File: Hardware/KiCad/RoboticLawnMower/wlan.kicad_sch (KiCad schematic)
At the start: 1 part, among them U3 ESP32-WROOM-32D

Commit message: Layout
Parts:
- added J16, J17: Conn_01x04, Connector_JST:JST_XA_B04B-XASK-1-A_1x04_P2.50mm_Vertical, symbol Connector_Generic:Conn_01x04
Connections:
- net GND: now reaches U3.1 (GND), U3.15 (GND), U3.38 (GND), U3.39 (GND)
- net GND: now also J16.4 (Pin_4), J17.4 (Pin_4)
- net RGB_LED_1: now reaches U3.13 (IO14)
- net RGB_LED_1: now also J17.3 (Pin_3)
- net RGB_LED_0: now reaches U3.16 (IO13)
- net RGB_LED_0: now also J17.2 (Pin_2)
- net +3.3V: now reaches U3.2 (VDD)
- net +3.3V: now also J16.1 (Pin_1), J17.1 (Pin_1)
- net at U3.26 (IO4): now also J16.2 (Pin_2)
- net at U3.29 (IO5): now also J16.3 (Pin_3)
- net UART_TxD_uC: now reaches U3.34 (RXD0/IO3)
- net UART_RxD_uC: now reaches U3.35 (TXD0/IO1)
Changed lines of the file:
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@@
 (kicad_sch (version 20211123) (generator eeschema)
   (paper "A3")
+  (junction (at 208.28 81.28) (diameter 0) (color 0 0 0 0)
+  )
+  (junction (at 209.55 59.69) (diameter 0) (color 0 0 0 0)
+  )
+  (wire (pts (xy 167.64 76.2) (xy 212.09 76.2))
+    (stroke (width 0) (type default) (color 0 0 0 0))
+  )
+  (wire (pts (xy 209.55 59.69) (xy 209.55 73.66))
+    (stroke (width 0) (type default) (color 0 0 0 0))
+  )
+  (wire (pts (xy 123.19 41.91) (xy 123.19 46.99))
+    (stroke (width 0) (type default) (color 0 0 0 0))
+  )
+  (wire (pts (xy 212.09 73.66) (xy 209.55 73.66))
+    (stroke (width 0) (type default) (color 0 0 0 0))
+  )
+  (wire (pts (xy 138.43 64.77) (xy 212.09 64.77))
+    (stroke (width 0) (type default) (color 0 0 0 0))
+  )
+  (wire (pts (xy 138.43 62.23) (xy 212.09 62.23))
+    (stroke (width 0) (type default) (color 0 0 0 0))
+  )
+  (wire (pts (xy 138.43 54.61) (xy 162.56 54.61))
+    (stroke (width 0) (type default) (color 0 0 0 0))
+  )
+  (wire (pts (xy 138.43 69.85) (xy 167.64 69.85))
+    (stroke (width 0) (type default) (color 0 0 0 0))
+  )
+  (wire (pts (xy 209.55 59.69) (xy 212.09 59.69))
+    (stroke (width 0) (type default) (color 0 0 0 0))
+  )
+  (wire (pts (xy 165.1 78.74) (xy 212.09 78.74))
+    (stroke (width 0) (type default) (color 0 0 0 0))
+  )
+  (wire (pts (xy 212.09 67.31) (xy 208.28 67.31))
+    (stroke (width 0) (type default) (color 0 0 0 0))
+  )
+  (wire (pts (xy 167.64 69.85) (xy 167.64 76.2))
+    (stroke (width 0) (type default) (color 0 0 0 0))
+  )
+  (wire (pts (xy 138.43 72.39) (xy 165.1 72.39))
+    (stroke (width 0) (type default) (color 0 0 0 0))
+  )
+  (wire (pts (xy 208.28 81.28) (xy 208.28 83.82))
+    (stroke (width 0) (type default) (color 0 0 0 0))
+  )
+  (wire (pts (xy 165.1 72.39) (xy 165.1 78.74))
+    (stroke (width 0) (type default) (color 0 0 0 0))
+  )
+  (wire (pts (xy 208.28 67.31) (xy 208.28 81.28))
+    (stroke (width 0) (type default) (color 0 0 0 0))
+  )
+  (wire (pts (xy 209.55 55.88) (xy 209.55 59.69))
+    (stroke (width 0) (type default) (color 0 0 0 0))
+  )
+  (wire (pts (xy 138.43 59.69) (xy 162.56 59.69))
+    (stroke (width 0) (type default) (color 0 0 0 0))
+  )
+  (wire (pts (xy 208.28 81.28) (xy 212.09 81.28))
+    (stroke (width 0) (type default) (color 0 0 0 0))
+  )
+  (label "RGB_LED_0" (at 172.72 76.2 0)
+    (effects (font (size 1.27 1.27)) (justify left bottom))
+  )
+  (label "RGB_LED_1" (at 172.72 78.74 0)
+    (effects (font (size 1.27 1.27)) (justify left bottom))
+  )
+  (hierarchical_label "UART_TxD_uC" (shape input) (at 162.56 59.69 0)
+    (effects (font (size 1.27 1.27)) (justify left))
+  )
+  (hierarchical_label "UART_RxD_uC" (shape input) (at 162.56 54.61 0)
+    (effects (font (size 1.27 1.27)) (justify left))
+  )
+  (symbol (lib_id "power:GND") (at 123.19 118.11 0) (unit 1)
+    (in_bom yes) (on_board yes) (fields_autoplaced)
+    (property "Reference" "#PWR087" (id 0) (at 123.19 124.46 0)
+      (effects (font (size 1.27 1.27)) hide)
+    )
+    (property "Value" "GND" (id 1) (at 123.19 123.19 0))
+    (property "Footprint" "" (id 2) (at 123.19 118.11 0)
+      (effects (font (size 1.27 1.27)) hide)
+    )
+    (property "Datasheet" "" (id 3) (at 123.19 118.11 0)
+      (effects (font (size 1.27 1.27)) hide)
+    )
+    (pin "1")
+  )
+  (symbol (lib_id "power:+3.3V") (at 209.55 55.88 0) (unit 1)
+    (in_bom yes) (on_board yes) (fields_autoplaced)
+    (property "Reference" "#PWR089" (id 0) (at 209.55 59.69 0)
+      (effects (font (size 1.27 1.27)) hide)
+    )
+    (property "Value" "+3.3V" (id 1) (at 209.55 50.8 0))
+    (property "Footprint" "" (id 2) (at 209.55 55.88 0)
+      (effects (font (size 1.27 1.27)) hide)
+    )
+    (property "Datasheet" "" (id 3) (at 209.55 55.88 0)
+      (effects (font (size 1.27 1.27)) hide)
+    )
+    (pin "1")
+  )
+  (symbol (lib_id "power:GND") (at 208.28 83.82 0) (unit 1)
+    (in_bom yes) (on_board yes) (fields_autoplaced)
+    (property "Reference" "#PWR088" (id 0) (at 208.28 90.17 0)
+      (effects (font (size 1.27 1.27)) hide)
+    )
+    (property "Value" "GND" (id 1) (at 208.28 88.9 0))
+    (property "Footprint" "" (id 2) (at 208.28 83.82 0)
+      (effects (font (size 1.27 1.27)) hide)
+    )
+    (property "Datasheet" "" (id 3) (at 208.28 83.82 0)
+      (effects (font (size 1.27 1.27)) hide)
+    )
+    (pin "1")
+  )
+  (symbol (lib_id "Connector_Generic:Conn_01x04") (at 217.17 76.2 0) (unit 1)
+    (in_bom yes) (on_board yes) (fields_autoplaced)
+    (property "Reference" "J17" (id 0) (at 219.71 76.1999 0)
+      (effects (font (size 1.27 1.27)) (justify left))
+    )
+    (property "Value" "Conn_01x04" (id 1) (at 219.71 78.7399 0)
+      (effects (font (size 1.27 1.27)) (justify left))
+    )
+    (property "Footprint" "Connector_JST:JST_XA_B04B-XASK-1-A_1x04_P2.50mm_Vertical" (id 2) (at 217.17 76.2 0)
+      (effects (font (size 1.27 1.27)) hide)
+    )
+    (property "Datasheet" "~" (id 3) (at 217.17 76.2 0)
+      (effects (font (size 1.27 1.27)) hide)
+    )
+    (pin "1")
+    (pin "2")
+    (pin "3")
+    (pin "4")
+  )
+  (symbol (lib_id "Connector_Generic:Conn_01x04") (at 217.17 62.23 0) (unit 1)
+    (in_bom yes) (on_board yes) (fields_autoplaced)
+    (property "Reference" "J16" (id 0) (at 219.71 62.2299 0)
+      (effects (font (size 1.27 1.27)) (justify left))
+    )
+    (property "Value" "Conn_01x04" (id 1) (at 219.71 64.7699 0)
+      (effects (font (size 1.27 1.27)) (justify left))
+    )
+    (property "Footprint" "Connector_JST:JST_XA_B04B-XASK-1-A_1x04_P2.50mm_Vertical" (id 2) (at 217.17 62.23 0)
+      (effects (font (size 1.27 1.27)) hide)
+    )
+    (property "Datasheet" "~" (id 3) (at 217.17 62.23 0)
+      (effects (font (size 1.27 1.27)) hide)
+    )
+    (pin "1")
+    (pin "2")
+    (pin "3")
+    (pin "4")
+  )
+  (symbol (lib_id "power:+3.3V") (at 123.19 41.91 0) (unit 1)
+    (in_bom yes) (on_board yes) (fields_autoplaced)
+    (property "Reference" "#PWR086" (id 0) (at 123.19 45.72 0)
+      (effects (font (size 1.27 1.27)) hide)
+    )
+    (property "Value" "+3.3V" (id 1) (at 123.19 36.83 0))
+    (property "Footprint" "" (id 2) (at 123.19 41.91 0)
+      (effects (font (size 1.27 1.27)) hide)
+    )
+    (property "Datasheet" "" (id 3) (at 123.19 41.91 0)
+      (effects (font (size 1.27 1.27)) hide)
+    )
+    (pin "1")
+  )
   (symbol (lib_id "RF_Module:ESP32-WROOM-32D") (at 123.19 82.55 0) (unit 1)
     (in_bom yes) (on_board yes) (fields_autoplaced)

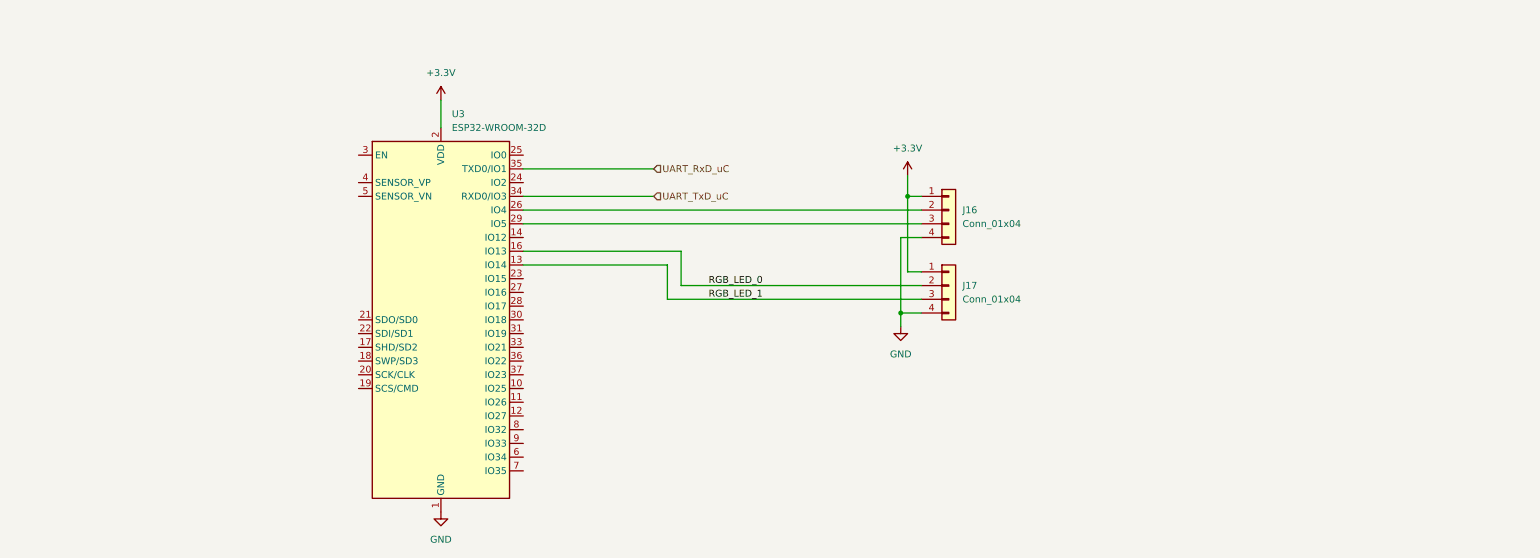
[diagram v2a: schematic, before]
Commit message: Schaltplan und Layout änderung
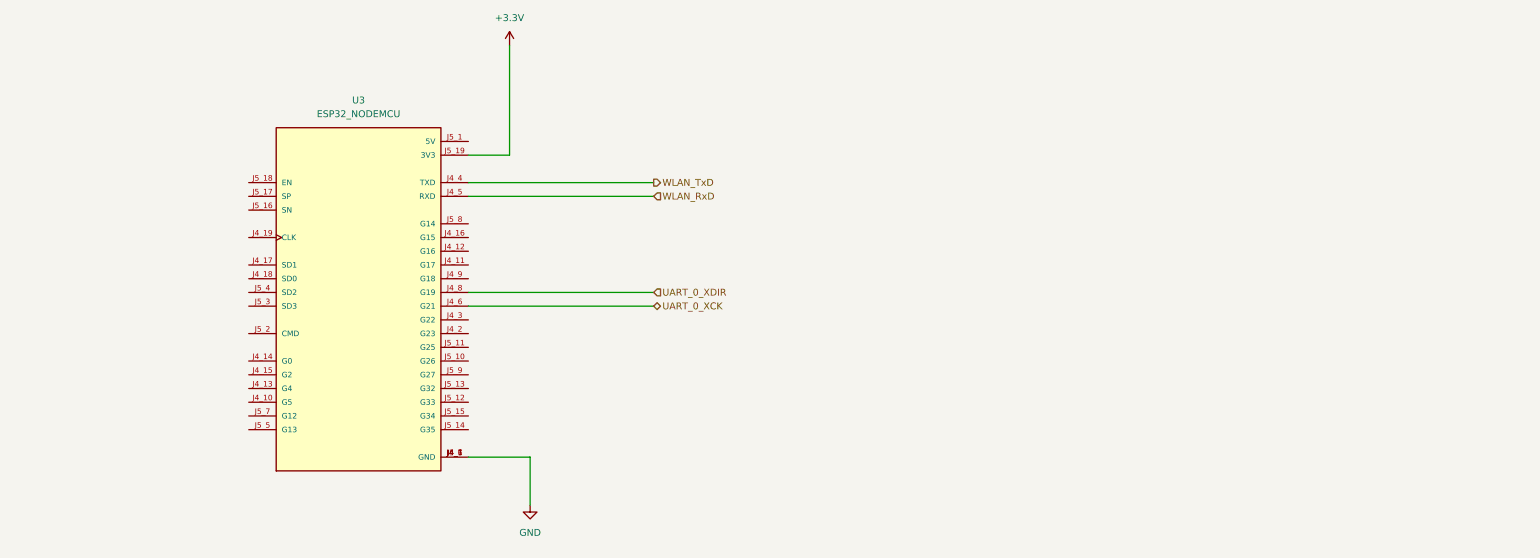
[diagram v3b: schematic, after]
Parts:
- removed J16, J17: Conn_01x04, Connector_JST:JST_XA_B04B-XASK-1-A_1x04_P2.50mm_Vertical, symbol Connector_Generic:Conn_01x04
- removed U3: ESP32-WROOM-32D, RF_Module:ESP32-WROOM-32, symbol RF_Module:ESP32-WROOM-32D
- added U3: ESP32_NODEMCU, MODULE_ESP32_NODEMCU, symbol ESP32_NODEMCU:ESP32_NODEMCU
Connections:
- net +3.3V: now also U3.J5_19 (3V3)
- net GND: now also U3.J4_1 (GND), U3.J4_7 (GND), U3.J5_6 (GND)
- new net UART_0_XCK: U3.J4_6 (G21)
- new net UART_0_XDIR: U3.J4_8 (G19)
- new net WLAN_RxD: U3.J4_5 (RXD)
- new net WLAN_TxD: U3.J4_4 (TXD)

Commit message: Layout
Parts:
- removed U3: ESP32_NODEMCU, MODULE_ESP32_NODEMCU, symbol ESP32_NODEMCU:ESP32_NODEMCU
- added U3: mini_esp32, ESP32_mini:ESP32_mini, symbol ESP_WEMOS_D1:mini_esp32
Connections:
- net +3.3V: now also U3.16 (3V3)
- net GND: now also U3.1 (GND), U3.22 (GND), U3.33 (GND)
- net UART_0_XCK: now also U3.28 (IO_32)
- net UART_0_XDIR: now also U3.24 (IO_27)
- net WLAN_RxD: now also U3.23 (RXD)
- net WLAN_TxD: now also U3.21 (TXD)
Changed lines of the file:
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@@
 (kicad_sch (version 20211123) (generator eeschema)
   (paper "A3")
-  (wire (pts (xy 128.27 77.47) (xy 162.56 77.47))
+  (junction (at 125.73 57.15) (diameter 0) (color 0 0 0 0)
+  )
+  (junction (at 125.73 59.69) (diameter 0) (color 0 0 0 0)
+  )
+  (wire (pts (xy 93.98 110.49) (xy 59.69 110.49))
     (stroke (width 0) (type default) (color 0 0 0 0))
   )
-  (wire (pts (xy 139.7 116.84) (xy 139.7 107.95))
+  (wire (pts (xy 125.73 59.69) (xy 125.73 116.84))
     (stroke (width 0) (type default) (color 0 0 0 0))
   )
-  (wire (pts (xy 135.89 31.75) (xy 135.89 52.07))
+  (wire (pts (xy 120.65 57.15) (xy 125.73 57.15))
     (stroke (width 0) (type default) (color 0 0 0 0))
   )
-  (wire (pts (xy 128.27 80.01) (xy 162.56 80.01))
+  (wire (pts (xy 125.73 31.75) (xy 125.73 52.07))
     (stroke (width 0) (type default) (color 0 0 0 0))
   )
-  (wire (pts (xy 128.27 57.15) (xy 162.56 57.15))
+  (wire (pts (xy 67.31 82.55) (xy 93.98 82.55))
     (stroke (width 0) (type default) (color 0 0 0 0))
   )
-  (wire (pts (xy 139.7 107.95) (xy 128.27 107.95))
+  (wire (pts (xy 125.73 54.61) (xy 125.73 57.15))
     (stroke (width 0) (type default) (color 0 0 0 0))
   )
-  (wire (pts (xy 128.27 52.07) (xy 135.89 52.07))
+  (wire (pts (xy 120.65 77.47) (xy 154.94 77.47))
     (stroke (width 0) (type default) (color 0 0 0 0))
   )
-  (wire (pts (xy 128.27 59.69) (xy 162.56 59.69))
+  (wire (pts (xy 59.69 100.33) (xy 67.31 100.33))
     (stroke (width 0) (type default) (color 0 0 0 0))
   )
-  (hierarchical_label "UART_0_XDIR" (shape input) (at 162.56 77.47 0)
+  (wire (pts (xy 67.31 100.33) (xy 67.31 82.55))
+    (stroke (width 0) (type default) (color 0 0 0 0))
+  )
+  (wire (pts (xy 120.65 54.61) (xy 125.73 54.61))
+    (stroke (width 0) (type default) (color 0 0 0 0))
+  )
+  (wire (pts (xy 120.65 52.07) (xy 125.73 52.07))
+    (stroke (width 0) (type default) (color 0 0 0 0))
+  )
+  (wire (pts (xy 125.73 57.15) (xy 125.73 59.69))
+    (stroke (width 0) (type default) (color 0 0 0 0))
+  )
+  (wire (pts (xy 120.65 80.01) (xy 154.94 80.01))
+    (stroke (width 0) (type default) (color 0 0 0 0))
+  )
+  (wire (pts (xy 120.65 59.69) (xy 125.73 59.69))
+    (stroke (width 0) (type default) (color 0 0 0 0))
+  )
+  (hierarchical_label "UART_0_XDIR" (shape input) (at 59.69 110.49 180)
+    (effects (font (size 1.27 1.27)) (justify right))
+  )
+  (hierarchical_label "UART_0_XCK" (shape bidirectional) (at 59.69 100.33 180)
+    (effects (font (size 1.27 1.27)) (justify right))
+  )
+  (hierarchical_label "WLAN_RxD" (shape input) (at 154.94 80.01 0)
     (effects (font (size 1.27 1.27)) (justify left))
   )
-  (hierarchical_label "UART_0_XCK" (shape bidirectional) (at 162.56 80.01 0)
+  (hierarchical_label "WLAN_TxD" (shape output) (at 154.94 77.47 0)
     (effects (font (size 1.27 1.27)) (justify left))
   )
-  (hierarchical_label "WLAN_RxD" (shape input) (at 162.56 59.69 0)
-    (effects (font (size 1.27 1.27)) (justify left))
-  )
-  (hierarchical_label "WLAN_TxD" (shape output) (at 162.56 57.15 0)
-    (effects (font (size 1.27 1.27)) (justify left))
-  )
-  (symbol (lib_id "power:GND") (at 139.7 116.84 0) (unit 1)
+  (symbol (lib_id "ESP_WEMOS_D1:mini_esp32") (at 106.68 46.99 0) (unit 1)
     (in_bom yes) (on_board yes) (fields_autoplaced)
-    (property "Reference" "#PWR0129" (id 0) (at 139.7 123.19 0)
+    (property "Reference" "U3" (id 0) (at 107.315 43.18 0))
+    (property "Value" "mini_esp32" (id 1) (at 107.315 45.72 0))
+    (property "Footprint" "ESP32_mini:ESP32_mini" (id 2) (at 110.49 44.45 0)
       (effects (font (size 1.27 1.27)) hide)
     )
-    (property "Value" "GND" (id 1) (at 139.7 121.92 0))
-    (property "Footprint" "" (id 2) (at 139.7 116.84 0)
+    (property "Datasheet" "" (id 3) (at 110.49 44.45 0)
       (effects (font (size 1.27 1.27)) hide)
     )
-    (property "Datasheet" "" (id 3) (at 139.7 116.84 0)
+    (pin "1")
+    (pin "2")
+    (pin "3")
+    (pin "4")
+    (pin "5")
+    (pin "10")
+    (pin "11")
+    (pin "12")
+    (pin "13")
+    (pin "14")
+    (pin "15")
+    (pin "16")
+    (pin "17")
+    (pin "18")
+    (pin "19")
+    (pin "20")
+    (pin "21")
+    (pin "22")
+    (pin "23")
+    (pin "24")
+    (pin "25")
+    (pin "26")
+    (pin "27")
+    (pin "28")
+    (pin "29")
+    (pin "30")
+    (pin "31")
+    (pin "32")
+    (pin "33")
+    (pin "34")
+    (pin "35")
+    (pin "36")
+    (pin "37")
+    (pin "38")
+    (pin "39")
+    (pin "40")
+    (pin "6")
+    (pin "7")
+    (pin "8")
+    (pin "9")
+  )
+  (symbol (lib_id "power:GND") (at 125.73 116.84 0) (unit 1)
+    (in_bom yes) (on_board yes) (fields_autoplaced)
+    (property "Reference" "#PWR0129" (id 0) (at 125.73 123.19 0)
+      (effects (font (size 1.27 1.27)) hide)
+    )
+    (property "Value" "GND" (id 1) (at 125.73 121.92 0))
+    (property "Footprint" "" (id 2) (at 125.73 116.84 0)
+      (effects (font (size 1.27 1.27)) hide)
+    )
+    (property "Datasheet" "" (id 3) (at 125.73 116.84 0)
       (effects (font (size 1.27 1.27)) hide)
     )
     (pin "1")
   )
-  (symbol (lib_id "power:+3.3V") (at 135.89 31.75 0) (unit 1)
+  (symbol (lib_id "power:+3.3V") (at 125.73 31.75 0) (unit 1)
     (in_bom yes) (on_board yes) (fields_autoplaced)
-    (property "Reference" "#PWR0130" (id 0) (at 135.89 35.56 0)
+    (property "Reference" "#PWR0130" (id 0) (at 125.73 35.56 0)
       (effects (font (size 1.27 1.27)) hide)
     )
-    (property "Value" "+3.3V" (id 1) (at 135.89 26.67 0))
-    (property "Footprint" "" (id 2) (at 135.89 31.75 0)
+    (property "Value" "+3.3V" (id 1) (at 125.73 26.67 0))
+    (property "Footprint" "" (id 2) (at 125.73 31.75 0)
       (effects (font (size 1.27 1.27)) hide)
     )
-    (property "Datasheet" "" (id 3) (at 135.89 31.75 0)
+    (property "Datasheet" "" (id 3) (at 125.73 31.75 0)
       (effects (font (size 1.27 1.27)) hide)
     )
     (pin "1")
   )
-  (symbol (lib_id "ESP32_NODEMCU:ESP32_NODEMCU") (at 107.95 77.47 0) (unit 1)
-    (in_bom yes) (on_board yes) (fields_autoplaced)
-    (property "Reference" "U3" (id 0) (at 107.95 41.91 0))
-    (property "Value" "ESP32_NODEMCU" (id 1) (at 107.95 44.45 0))
-    (property "Footprint" "MODULE_ESP32_NODEMCU" (id 2) (at 107.95 77.47 0)
-      (effects (font (size 1.27 1.27)) (justify bottom) hide)
-    )
-    (property "Datasheet" "" (id 3) (at 107.95 77.47 0)
-      (effects (font (size 1.27 1.27)) hide)
-    )
-    (property "STANDARD" "Manufacturer Recommendations" (id 4) (at 107.95 77.47 0)
-      (effects (font (size 1.27 1.27)) (justify bottom) hide)
-    )
-    (property "MANUFACTURER" "Espressif" (id 5) (at 107.95 77.47 0)
-      (effects (font (size 1.27 1.27)) (justify bottom) hide)
-    )
-    (property "MAXIMUM_PACKAGE_HEIGHT" "6.6 mm" (id 6) (at 107.95 77.47 0)
-      (effects (font (size 1.27 1.27)) (justify bottom) hide)
-    )
-    (pin "J4_1")
-    (pin "J4_10")
-    (pin "J4_11")
-    (pin "J4_12")
-    (pin "J4_13")
-    (pin "J4_14")
-    (pin "J4_15")
-    (pin "J4_16")
-    (pin "J4_17")
-    (pin "J4_18")
-    (pin "J4_19")
-    (pin "J4_2")
-    (pin "J4_3")
-    (pin "J4_4")
-    (pin "J4_5")
-    (pin "J4_6")
-    (pin "J4_7")
-    (pin "J4_8")
-    (pin "J4_9")
-    (pin "J5_1")
-    (pin "J5_10")
-    (pin "J5_11")
-    (pin "J5_12")
-    (pin "J5_13")
-    (pin "J5_14")
-    (pin "J5_15")
-    (pin "J5_16")
-    (pin "J5_17")
-    (pin "J5_18")
-    (pin "J5_19")
-    (pin "J5_2")
-    (pin "J5_3")
-    (pin "J5_4")
-    (pin "J5_5")
-    (pin "J5_6")
-    (pin "J5_7")
-    (pin "J5_8")
-    (pin "J5_9")
-  )
 )
